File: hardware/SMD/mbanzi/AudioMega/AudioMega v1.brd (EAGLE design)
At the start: 60 x 58 mm, 75 parts, among them Q1 BC846ASMD, Q2 BC846ASMD, Q3 BC846ASMD, Q4 2N7002, Q5 BC846ASMD, Q6 BC846ASMD, U1 REG1117-5, U2 REG1117-3.3, U3 ATMEGA328-AU, U4 LM386M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

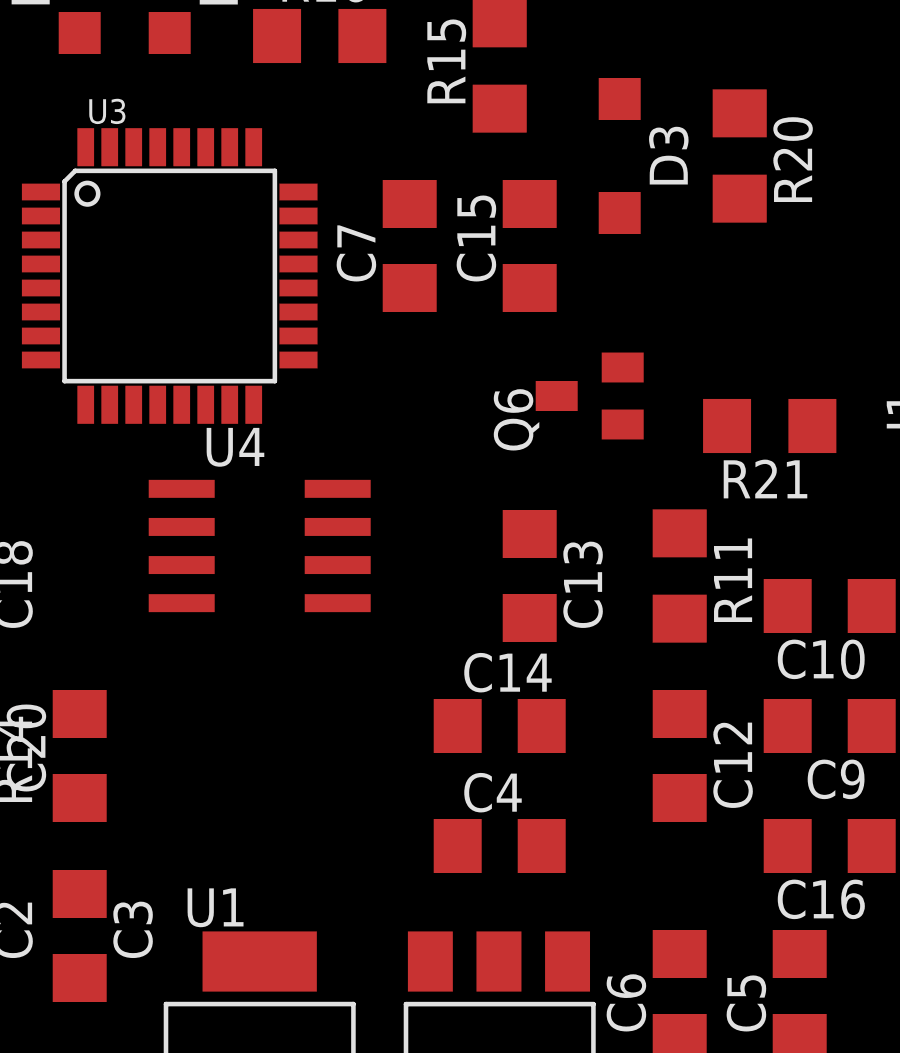
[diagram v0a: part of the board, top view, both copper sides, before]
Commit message: Updated: - Beeper connected to M64 (base of beeper transistor) - R10 changed to 33k - deleted some capasitors
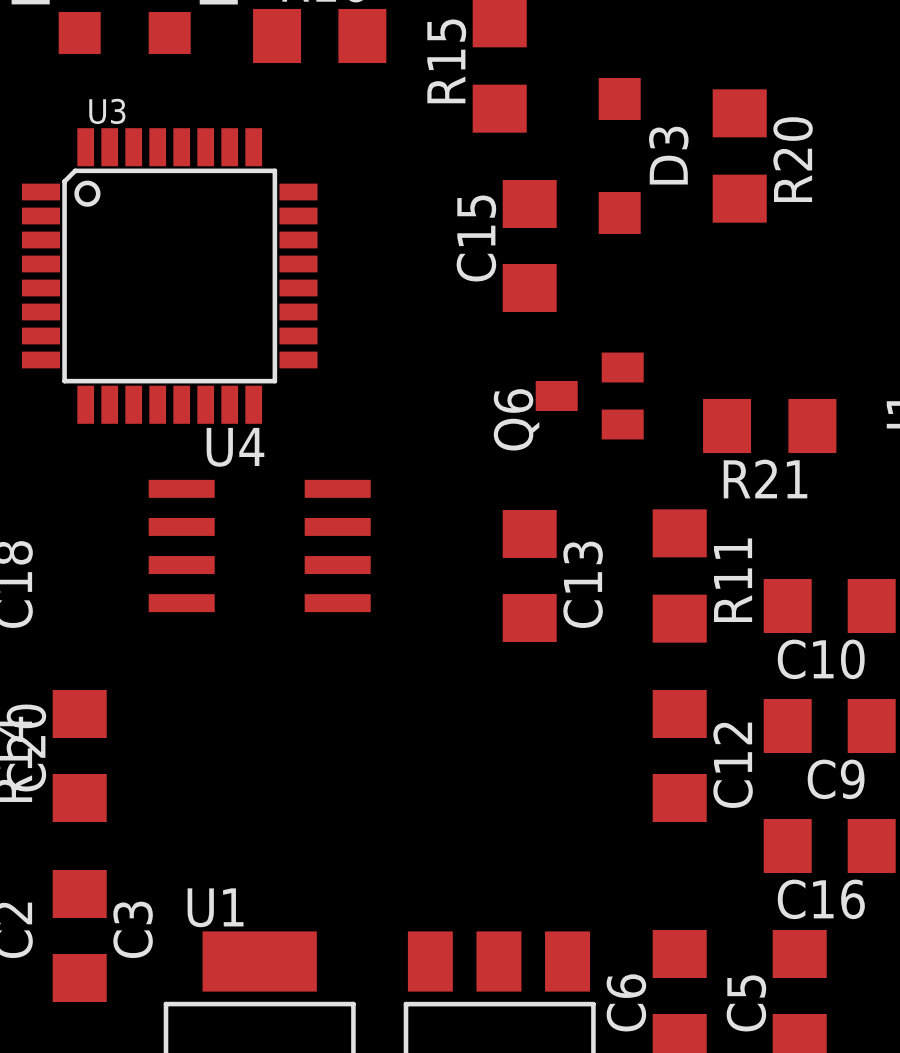
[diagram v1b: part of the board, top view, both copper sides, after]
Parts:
- removed C14, C4: 10uF, resistor:C1206
- removed C7: 100nF, resistor:C1206
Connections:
- net +3V3: no longer C7.1
- net +5V: no longer C14.1, C4.1
- net GND: no longer C14.2, C4.2, C7.2
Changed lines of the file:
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@@
 <element name="C2" library="resistor" package="C1206" value="100nF" x="23" y="11" rot="R270"/>
 <element name="C3" library="resistor" package="C1206" value="10uF" x="27" y="11" rot="R270"/>
-<element name="C4" library="resistor" package="C1206" value="10uF" x="41" y="14"/>
 <element name="C5" library="resistor" package="C1206" value="100nF" x="51" y="9" rot="R90"/>
 <element name="C6" library="resistor" package="C1206" value="10uF" x="47" y="9" rot="R90"/>
-<element name="C7" library="resistor" package="C1206" value="100nF" x="38" y="34" rot="R90"/>
 <element name="C8" library="resistor" package="C1206" value="100nF" x="11" y="23" rot="R90"/>
 <element name="C9" library="resistor" package="C1206" value="100uF" x="52" y="18" rot="R180"/>
@@
 <element name="C12" library="resistor" package="C1206" value="47nF" x="47" y="17" rot="R270"/>
 <element name="C13" library="resistor" package="C1206" value="100nF" x="42" y="23" rot="R270"/>
-<element name="C14" library="resistor" package="C1206" value="10uF" x="41" y="18"/>
 <element name="C15" library="resistor" package="C1206" value="100nF" x="42" y="34" rot="R90"/>
 <element name="C16" library="resistor" package="C1206" value="47uF" x="52" y="14" rot="R180"/>
@@
 <contactref element="J1" pad="6"/>
 <contactref element="U4" pad="4"/>
-<contactref element="C14" pad="2"/>
 <contactref element="C13" pad="2"/>
 <contactref element="R14" pad="1"/>
@@
 <contactref element="C2" pad="2"/>
 <contactref element="C3" pad="2"/>
-<contactref element="C4" pad="2"/>
 <contactref element="U2" pad="1"/>
 <contactref element="C5" pad="2"/>
@@
 <contactref element="JP17" pad="1"/>
 <contactref element="Q2" pad="2"/>
-<contactref element="C7" pad="2"/>
 <contactref element="Q1" pad="2"/>
 <contactref element="D3" pad="A"/>
@@
 <wire x1="45" y1="35.1" x2="49" y2="35.578" width="0" layer="19" extent="1-1"/>
 <wire x1="42" y1="35.4" x2="45" y2="35.1" width="0" layer="19" extent="1-1"/>
-<wire x1="38" y1="35.4" x2="42" y2="35.4" width="0" layer="19" extent="1-1"/>
-<wire x1="34.2926" y1="33.4" x2="38" y2="35.4" width="0" layer="19" extent="1-1"/>
 <wire x1="45.1" y1="29.95" x2="45" y2="35.1" width="0" layer="19" extent="1-1"/>
 <wire x1="47" y1="24.422" x2="45.1" y2="29.95" width="0" layer="19" extent="1-1"/>
 <wire x1="42" y1="21.6" x2="47" y2="24.422" width="0" layer="19" extent="1-1"/>
-<wire x1="42.4" y1="18" x2="42" y2="21.6" width="0" layer="19" extent="1-1"/>
-<wire x1="42.4" y1="14" x2="42.4" y2="18" width="0" layer="19" extent="1-1"/>
-<wire x1="43.2606" y1="10.1496" x2="42.4" y2="14" width="0" layer="19" extent="1-1"/>
-<wire x1="47" y1="10.4" x2="43.2606" y2="10.1496" width="0" layer="19" extent="1-1"/>
-<wire x1="51" y1="10.4" x2="47" y2="10.4" width="0" layer="19" extent="1-1"/>
-<wire x1="57" y1="5" x2="51" y2="10.4" width="0" layer="19" extent="1-1"/>
+<wire x1="34.2926" y1="33.4" x2="42" y2="35.4" width="0" layer="19" extent="1-1"/>
 <wire x1="25.7074" y1="34.2" x2="34.2926" y2="33.4" width="0" layer="19" extent="1-1"/>
 <wire x1="25.7074" y1="32.6" x2="25.7074" y2="34.2" width="0" layer="19" extent="1-1"/>
-<wire x1="37.95" y1="45.9" x2="38" y2="35.4" width="0" layer="19" extent="1-1"/>
+<wire x1="37.95" y1="45.9" x2="42" y2="35.4" width="0" layer="19" extent="1-1"/>
 <wire x1="23" y1="21.6" x2="25.7074" y2="32.6" width="0" layer="19" extent="1-1"/>
 <wire x1="23" y1="18.422" x2="23" y2="21.6" width="0" layer="19" extent="1-1"/>
@@
 <wire x1="23" y1="6.4" x2="23" y2="9.6" width="0" layer="19" extent="1-1"/>
 <wire x1="30.7394" y1="3.8504" x2="27" y2="9.6" width="0" layer="19" extent="1-1"/>
+<wire x1="43.2606" y1="10.1496" x2="42" y2="21.6" width="0" layer="19" extent="1-1"/>
+<wire x1="47" y1="10.4" x2="43.2606" y2="10.1496" width="0" layer="19" extent="1-1"/>
+<wire x1="51" y1="10.4" x2="47" y2="10.4" width="0" layer="19" extent="1-1"/>
+<wire x1="57" y1="5" x2="51" y2="10.4" width="0" layer="19" extent="1-1"/>
 <wire x1="16.6" y1="42" x2="25.7074" y2="34.2" width="0" layer="19" extent="1-1"/>
 <wire x1="12.4" y1="42" x2="16.6" y2="42" width="0" layer="19" extent="1-1"/>
@@
 <signal name="+5V">
 <contactref element="U4" pad="6"/>
-<contactref element="C14" pad="1"/>
 <contactref element="U1" pad="2"/>
 <contactref element="U2" pad="3"/>
 <contactref element="C2" pad="1"/>
 <contactref element="C3" pad="1"/>
-<contactref element="C4" pad="1"/>
 <contactref element="JP3" pad="1"/>
 <contactref element="R18" pad="1"/>
 <wire x1="35.6" y1="23.365" x2="41" y2="45.578" width="0" layer="19" extent="1-1"/>
-<wire x1="39.6" y1="18" x2="35.6" y2="23.365" width="0" layer="19" extent="1-1"/>
-<wire x1="39.6" y1="14" x2="39.6" y2="18" width="0" layer="19" extent="1-1"/>
-<wire x1="38.6886" y1="10.1496" x2="39.6" y2="14" width="0" layer="19" extent="1-1"/>
+<wire x1="38.6886" y1="10.1496" x2="35.6" y2="23.365" width="0" layer="19" extent="1-1"/>
 <wire x1="33.0254" y1="3.8504" x2="38.6886" y2="10.1496" width="0" layer="19" extent="1-1"/>
 <wire x1="27" y1="12.4" x2="33.0254" y2="3.8504" width="0" layer="19" extent="1-1"/>
@@
 <contactref element="C5" pad="1"/>
 <contactref element="C6" pad="1"/>
-<contactref element="C7" pad="1"/>
 <contactref element="Q4" pad="3"/>
 <wire x1="42" y1="32.6" x2="57" y2="39.27" width="0" layer="19" extent="1-1"/>
-<wire x1="38" y1="32.6" x2="42" y2="32.6" width="0" layer="19" extent="1-1"/>
-<wire x1="34.2926" y1="32.6" x2="38" y2="32.6" width="0" layer="19" extent="1-1"/>
+<wire x1="34.2926" y1="32.6" x2="42" y2="32.6" width="0" layer="19" extent="1-1"/>
 <wire x1="34.2926" y1="31" x2="34.2926" y2="32.6" width="0" layer="19" extent="1-1"/>
 <wire x1="25.7074" y1="33.4" x2="34.2926" y2="32.6" width="0" layer="19" extent="1-1"/>

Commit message: Updated: Maked in corresponding of last hageha version. - changed R09, not r10, to 33k.
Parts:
- R10: value 33k -> 4k7
- R14: value 330 -> 1k
- R9: value 100k -> 33k
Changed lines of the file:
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@@
 <element name="R7" library="resistor" package="R1206" value="1k" x="7" y="29" rot="R90"/>
 <element name="R8" library="resistor" package="R1206" value="560k" x="11" y="29" rot="R90"/>
-<element name="R9" library="resistor" package="R1206" value="100k" x="15" y="23" rot="R270"/>
-<element name="R10" library="resistor" package="R1206" value="33k" x="19" y="23" rot="R90"/>
+<element name="R9" library="resistor" package="R1206" value="33k" x="15" y="23" rot="R270"/>
+<element name="R10" library="resistor" package="R1206" value="4k7" x="19" y="23" rot="R90"/>
 <element name="R11" library="resistor" package="R1206" value="10" x="47" y="23" rot="R270"/>
 <element name="R12" library="resistor" package="R1206" value="470k" x="15" y="29" rot="R90"/>
 <element name="R13" library="resistor" package="R1206" value="100k" x="57" y="23" rot="R90"/>
-<element name="R14" library="resistor" package="R1206" value="330" x="23" y="17" rot="R270"/>
+<element name="R14" library="resistor" package="R1206" value="1k" x="23" y="17" rot="R270"/>
 <element name="R15" library="resistor" package="R1206" value="2k2" x="41" y="40" rot="R90"/>
 <element name="R16" library="resistor" package="R1206" value="1k" x="35" y="41"/>
